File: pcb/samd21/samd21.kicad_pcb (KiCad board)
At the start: 2 copper layers, 12 parts, among them SW1 SW_Push, U1 TLV70033_SOT23-5, U2 ATSAMD21E17A-A

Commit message: v1-dev pcb+schem complete. not finished
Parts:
- added J1: Conn_01x04_Male, Connector_PinSocket_2.54mm:PinSocket_1x04_P2.54mm_Vertical, F.Cu at (93.7, 72.0)
- moved U1 51.4 mm to (111.3, 54.3)
- moved C2 51.1 mm to (106.8, 54.3), turned to 270 degrees
- moved C3 49.2 mm to (115.7, 54.3), turned to 270 degrees
- moved D1 48.2 mm to (94.6, 65.3)
- moved USB1 47.1 mm to (93.0, 57.9)
- moved R1 44.4 mm to (100.1, 65.3), turned to 180 degrees
- moved C1 39.5 mm to (97.3, 67.6)
- moved SW1 39.3 mm to (114.0, 59.2)
- moved U2 29.7 mm to (111.3, 67.7), turned to 90 degrees
- moved MX1 24.3 mm to (129.4, 62.7)
- moved MX2 23.5 mm to (148.5, 62.7)
- moved MX3 22.9 mm to (167.5, 62.7)
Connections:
- net Net-(C2-Pad1) renamed /5V
- U2 pad 11: KEY3 -> Net-(U2-Pad11)
- U2 pad 13: Net-(R1-Pad1) -> Net-(U2-Pad13)
- U2 pad 25: Net-(U2-Pad25) -> Net-(R1-Pad1)
- U2 pad 6: Net-(U2-Pad6) -> KEY3
- U2 pad 7: KEY1 -> KEY2
- U2 pad 8: KEY2 -> KEY1
- USB1 pad 6: Net-(USB1-Pad6) -> GND
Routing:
- net +3V3: track 0.00 -> 122.2 mm, vias 0 -> 2
- net GND: track 0.00 -> 106.4 mm
- net KEY3: track 0.00 -> 68.3 mm
- net KEY2: track 0.00 -> 48.1 mm
- net KEY1: track 0.00 -> 31.9 mm
- net /5V: track 0.00 -> 18.2 mm
- net D-: track 0.00 -> 15.5 mm
- net D+: track 0.00 -> 14.7 mm
- net Net-(SW1-Pad2): track 0.00 -> 12.4 mm, vias 0 -> 2
- net SWCLK: track 0.00 -> 11.7 mm
- net SWDIO: track 0.00 -> 9.69 mm
- net Net-(C1-Pad2): track 0.00 -> 8.92 mm
- net Net-(R1-Pad1): track 0.00 -> 6.87 mm
- net Net-(D1-Pad2): track 0.00 -> 3.63 mm
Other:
- board outline added: 86.5 x 23 mm
- net class Default: trace_width 0.25 -> 0.254
- net class Power added: clearance 0.2, trace_width 0.381, via_dia 0.8, via_drill 0.4
- board text added: "three.mee42.dev"
- board text added: "v1-dev"

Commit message: v1!
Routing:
- net +3V3: track 122.2 -> 110.3 mm
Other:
- board text added: "JLCJLCJLCJLC"
- board text added: "v1"
- board text removed: "v1-dev"
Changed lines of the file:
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@@
     (thickness 1.6)
     (drawings 13)
-    (tracks 134)
+    (tracks 128)
     (zones 0)
     (modules 13)
@@
       (plotinvisibletext false)
       (padsonsilk false)
-      (subtractmaskfromsilk false)
+      (subtractmaskfromsilk true)
       (outputformat 1)
       (mirror false)
-      (drillshape 1)
+      (drillshape 0)
       (scaleselection 1)
-      (outputdirectory ""))
+      (outputdirectory "../../build/"))
   )
   (net 0 "")
@@
       (effects (font (size 0.5 0.5) (thickness 0.08)))
     )
-    (pad 2 smd roundrect (at 0.9125 0 180) (size 1.025 1.4) (layers F.Cu F.Paste F.Mask) (roundrect_rratio 0.243902)
+    (pad 2 smd roundrect (at 0.9125 0 180) (size 1.025 1.4) (layers F.Cu F.Paste F.Mask) (roundrect_rratio 0.2439014634146341)
       (net 4 "Net-(D1-Pad2)"))
-    (pad 1 smd roundrect (at -0.9125 0 180) (size 1.025 1.4) (layers F.Cu F.Paste F.Mask) (roundrect_rratio 0.243902)
+    (pad 1 smd roundrect (at -0.9125 0 180) (size 1.025 1.4) (layers F.Cu F.Paste F.Mask) (roundrect_rratio 0.2439014634146341)
       (net 8 "Net-(R1-Pad1)"))
     (model ${KISYS3DMOD}/Resistor_SMD.3dshapes/R_0805_2012Metric.wrl
@@
     )
   )
-  (gr_text "v1-dev\n" (at 159.512 73.406) (layer F.SilkS)
+  (gr_text JLCJLCJLCJLC (at 152.273 73.533) (layer F.SilkS)
     (effects (font (size 1 1) (thickness 0.15)))
   )
-  (gr_text three.mee42.dev (at 170.815 73.406) (layer F.SilkS)
+  (gr_text "v1\n\n" (at 160.528 74.295) (layer F.SilkS)
     (effects (font (size 1 1) (thickness 0.15)))
   )
-  (dimension 0.762 (width 0.15) (layer Dwgs.User)
-    (gr_text "0.762 mm" (at 122.077 70.104 270) (layer Dwgs.User)
-      (effects (font (size 1 1) (thickness 0.15)))
-    )
-    (feature1 (pts (xy 115.57 70.485) (xy 121.363421 70.485)))
-    (feature2 (pts (xy 115.57 69.723) (xy 121.363421 69.723)))
-    (crossbar (pts (xy 120.777 69.723) (xy 120.777 70.485)))
-    (arrow1a (pts (xy 120.777 70.485) (xy 120.190579 69.358496)))
-    (arrow1b (pts (xy 120.777 70.485) (xy 121.363421 69.358496)))
-    (arrow2a (pts (xy 120.777 69.723) (xy 120.190579 70.849504)))
-    (arrow2b (pts (xy 120.777 69.723) (xy 121.363421 70.849504)))
+  (gr_text three.mee42.dev (at 169.545 73.533) (layer F.SilkS)
+    (effects (font (size 1 1) (thickness 0.15)))
   )
   (dimension 86.522391 (width 0.15) (layer Dwgs.User)
@@
   (segment (start 93.726 72.009) (end 96.774 68.961) (width 0.381) (layer F.Cu) (net 3))
   (segment (start 126.325501 59.288499) (end 126.89 58.724) (width 0.381) (layer F.Cu) (net 3))
-  (segment (start 143.313892 56.088892) (end 145.963 58.738) (width 0.381) (layer F.Cu) (net 3))
-  (segment (start 142.702892 56.088892) (end 143.313892 56.088892) (width 0.381) (layer F.Cu) (net 3))
-  (segment (start 129.675108 56.088892) (end 142.702892 56.088892) (width 0.381) (layer F.Cu) (net 3))
-  (segment (start 162.377892 56.102892) (end 165.013 58.738) (width 0.381) (layer F.Cu) (net 3))
-  (segment (start 142.716892 56.102892) (end 162.377892 56.102892) (width 0.381) (layer F.Cu) (net 3))
-  (segment (start 142.702892 56.088892) (end 142.716892 56.102892) (width 0.381) (layer F.Cu) (net 3))
   (via (at 118.364 59.309) (size 0.8) (drill 0.4) (layers F.Cu B.Cu) (net 3))
   (segment (start 117.348 59.309) (end 118.364 59.309) (width 0.381) (layer B.Cu) (net 3))
@@
   (segment (start 118.763999 59.708999) (end 118.763999 61.569903) (width 0.381) (layer F.Cu) (net 3))
   (segment (start 118.364 59.309) (end 118.763999 59.708999) (width 0.381) (layer F.Cu) (net 3))
-  (segment (start 118.364 59.309) (end 121.584108 56.088892) (width 0.381) (layer F.Cu) (net 3))
-  (segment (start 124.254892 56.088892) (end 126.89 58.724) (width 0.381) (layer F.Cu) (net 3))
-  (segment (start 123.779892 56.088892) (end 124.254892 56.088892) (width 0.381) (layer F.Cu) (net 3))
-  (segment (start 129.675108 56.088892) (end 123.779892 56.088892) (width 0.381) (layer F.Cu) (net 3))
-  (segment (start 123.779892 56.088892) (end 121.584108 56.088892) (width 0.381) (layer F.Cu) (net 3))
+  (segment (start 144.639 60.184) (end 144.653 60.198) (width 0.381) (layer B.Cu) (net 3))
+  (segment (start 125.58 60.184) (end 144.639 60.184) (width 0.381) (layer B.Cu) (net 3))
+  (segment (start 144.653 60.198) (end 163.703 60.198) (width 0.381) (layer B.Cu) (net 3))
+  (segment (start 119.239 60.184) (end 118.364 59.309) (width 0.381) (layer B.Cu) (net 3))
+  (segment (start 125.58 60.184) (end 119.239 60.184) (width 0.381) (layer B.Cu) (net 3))
   (segment (start 99.187 65.278) (end 95.5525 65.278) (width 0.254) (layer F.Cu) (net 4))
   (segment (start 114.724991 72.613991) (end 114.052 71.941) (width 0.254) (layer F.Cu) (net 5))

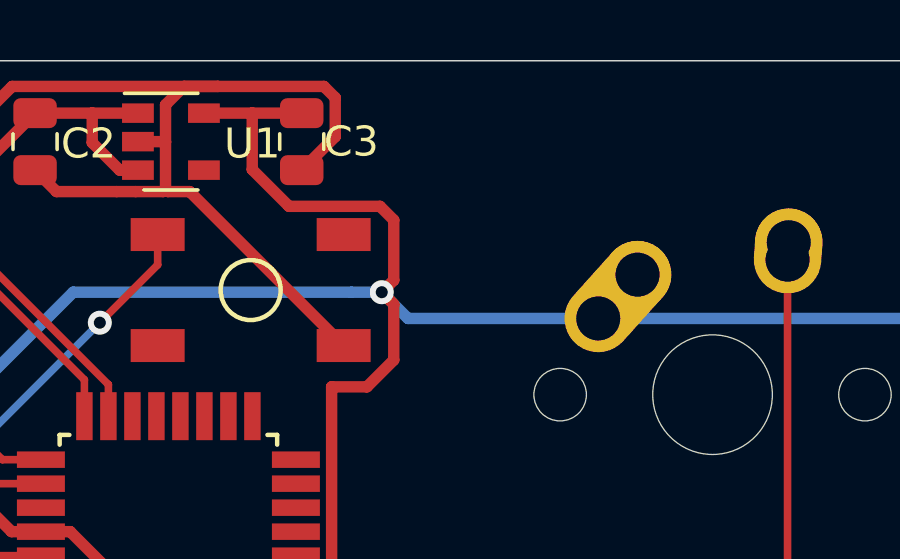
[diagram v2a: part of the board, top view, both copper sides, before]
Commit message: moved switches from 3v3 to GND, using pullup
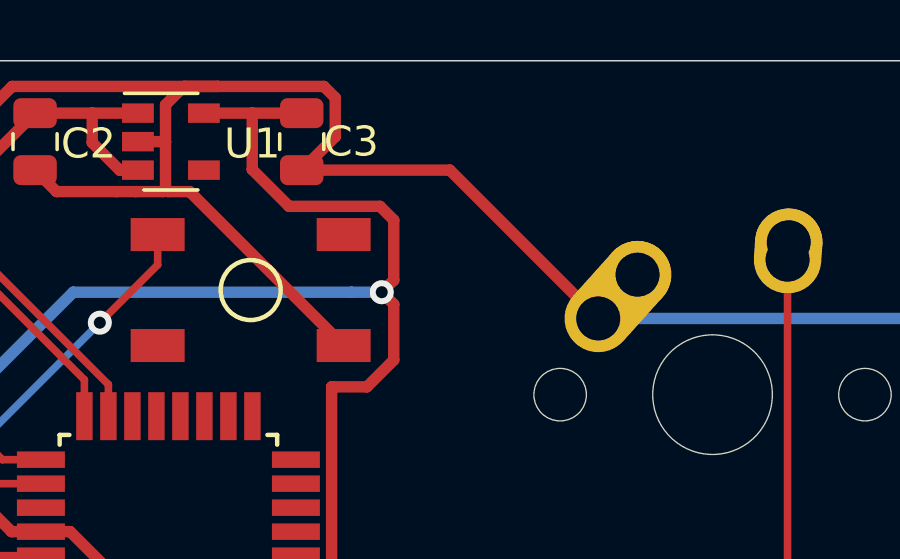
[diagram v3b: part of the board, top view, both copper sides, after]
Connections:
- MX1 pad 1: +3V3 -> GND
- MX2 pad 1: +3V3 -> GND
- MX3 pad 1: +3V3 -> GND
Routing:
- net GND: track 106.4 -> 157.2 mm
- net +3V3: track 110.3 -> 63.8 mm

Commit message: playing around with v2 board ideas
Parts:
- removed SW1: SW_Push, random_parts2:SKQG-1155865
- added 2: LED, LED_SMD:LED_0805_2012Metric_Castellated, F.Cu at (105.5, 59.8)
- added 3: LED, LED_SMD:LED_0805_2012Metric_Castellated, F.Cu at (105.5, 61.8)
- added 4: LED, LED_SMD:LED_0805_2012Metric_Castellated, F.Cu at (105.5, 63.8)
- added 5: LED, LED_SMD:LED_0805_2012Metric_Castellated, F.Cu at (105.5, 65.8)
- added D6: LED, LED_SMD:LED_0805_2012Metric_Castellated, F.Cu at (95.3, 67.0)
- added GND: TestPoint, TestPoint:TestPoint_Pad_1.0x1.0mm, F.Cu at (114.2, 54.5)
- added R2: 1.5K, Resistor_SMD:R_0805_2012Metric_Pad1.20x1.40mm_HandSolder, F.Cu at (101.8, 60.8)
- added R3: 1.5K, Resistor_SMD:R_0805_2012Metric_Pad1.20x1.40mm_HandSolder, F.Cu at (101.8, 62.5)
- added R4: 1.5K, Resistor_SMD:R_0805_2012Metric_Pad1.20x1.40mm_HandSolder, F.Cu at (101.8, 64.5)
- added R5: 1.5K, Resistor_SMD:R_0805_2012Metric_Pad1.20x1.40mm_HandSolder, F.Cu at (101.8, 66.5)
- added R6: 1.5K, Resistor_SMD:R_0805_2012Metric_Pad1.20x1.40mm_HandSolder, F.Cu at (95.2, 64.8)
- added RST: TestPoint, TestPoint:TestPoint_Pad_1.0x1.0mm, F.Cu at (106.8, 69.8)
- 1: renamed from D1; value red LED -> LED; footprint LED_SMD:LED_0805_2012Metric -> LED_SMD:LED_0805_2012Metric_Castellated
- R1: footprint Resistor_SMD:R_0805_2012Metric -> Resistor_SMD:R_0805_2012Metric_Pad1.20x1.40mm_HandSolder
- moved 1 16.5 mm to (109.5, 58.2)
- moved C1 7.73 mm to (104.2, 71.0), turned to -90 degrees
- moved R1 6.73 mm to (101.8, 58.8)
- moved C3 4.75 mm to (111.0, 55.0)
- moved U1 4.56 mm to (106.8, 55.1)
- moved C2 4.39 mm to (102.5, 55.1)
- moved U2 2.97 mm to (113.5, 65.8), turned to 180 degrees
- moved J1 0.28 mm to (93.7, 71.7)
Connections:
- 1 pad 1: GND -> Net-(D1-Pad1)
- 1 pad 2: Net-(D1-Pad2) -> LED0
- R1 pad 1: Net-(R1-Pad1) -> Net-(D1-Pad1)
- R1 pad 2: Net-(D1-Pad2) -> GND
- U1 pad 4: Net-(U1-Pad4) -> unconnected-(U1-Pad4)
- U2 pad 1: Net-(U2-Pad1) -> unconnected-(U2-Pad1)
- U2 pad 11: Net-(U2-Pad11) -> unconnected-(U2-Pad11)
- U2 pad 12: Net-(U2-Pad12) -> unconnected-(U2-Pad12)
- U2 pad 13: Net-(U2-Pad13) -> unconnected-(U2-Pad13)
- U2 pad 14: Net-(U2-Pad14) -> unconnected-(U2-Pad14)
- U2 pad 15: Net-(U2-Pad15) -> LED0
- U2 pad 16: Net-(U2-Pad16) -> LED1
- U2 pad 17: Net-(U2-Pad17) -> LED2
- U2 pad 18: Net-(U2-Pad18) -> LED3
- U2 pad 19: Net-(U2-Pad19) -> LED4
- U2 pad 2: Net-(U2-Pad2) -> unconnected-(U2-Pad2)
- U2 pad 20: Net-(U2-Pad20) -> unconnected-(U2-Pad20)
- U2 pad 21: Net-(U2-Pad21) -> unconnected-(U2-Pad21)
- U2 pad 22: Net-(U2-Pad22) -> LED5
- U2 pad 25: Net-(R1-Pad1) -> unconnected-(U2-Pad25)
- U2 pad 27: Net-(U2-Pad27) -> unconnected-(U2-Pad27)
- U2 pad 3: Net-(U2-Pad3) -> unconnected-(U2-Pad3)
- U2 pad 4: Net-(U2-Pad4) -> unconnected-(U2-Pad4)
- U2 pad 5: Net-(U2-Pad5) -> unconnected-(U2-Pad5)
- USB1 pad 2: Net-(USB1-Pad2) -> unconnected-(USB1-Pad2)
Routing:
- net D+: track 14.7 -> 34.7 mm
- net SWDIO: track 9.69 -> 29.5 mm
- net D-: track 15.5 -> 34.1 mm
- net +3V3: track 63.8 -> 48.0 mm, vias 2 -> 0
- net LED5: track 0.00 -> 13.5 mm
- net KEY1: track 31.9 -> 21.0 mm
- net SWCLK: track 11.7 -> 22.1 mm
- net KEY3: track 68.3 -> 59.5 mm
- net GND: track 157.2 -> 165.4 mm
- net KEY2: track 48.1 -> 40.4 mm
- net Net-(R1-Pad1): track 6.87 -> 0.00 mm
- net Net-(U2-Pad26): track 12.4 -> 6.44 mm, vias 2 -> 0
- net Net-(D1-Pad1): track 0.00 -> 5.83 mm
- net LED1: track 0.00 -> 5.30 mm
- net Net-(D1-Pad2): track 3.63 -> 0.00 mm
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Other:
- net class Default removed
- net class Power removed
- board text added: "v2"
- board text removed: "v1"
